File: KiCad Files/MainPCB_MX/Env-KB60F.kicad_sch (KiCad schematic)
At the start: 157 parts, among them J1 Conn_01x04, SW1 EVQ-P7A01P, U1 Pico

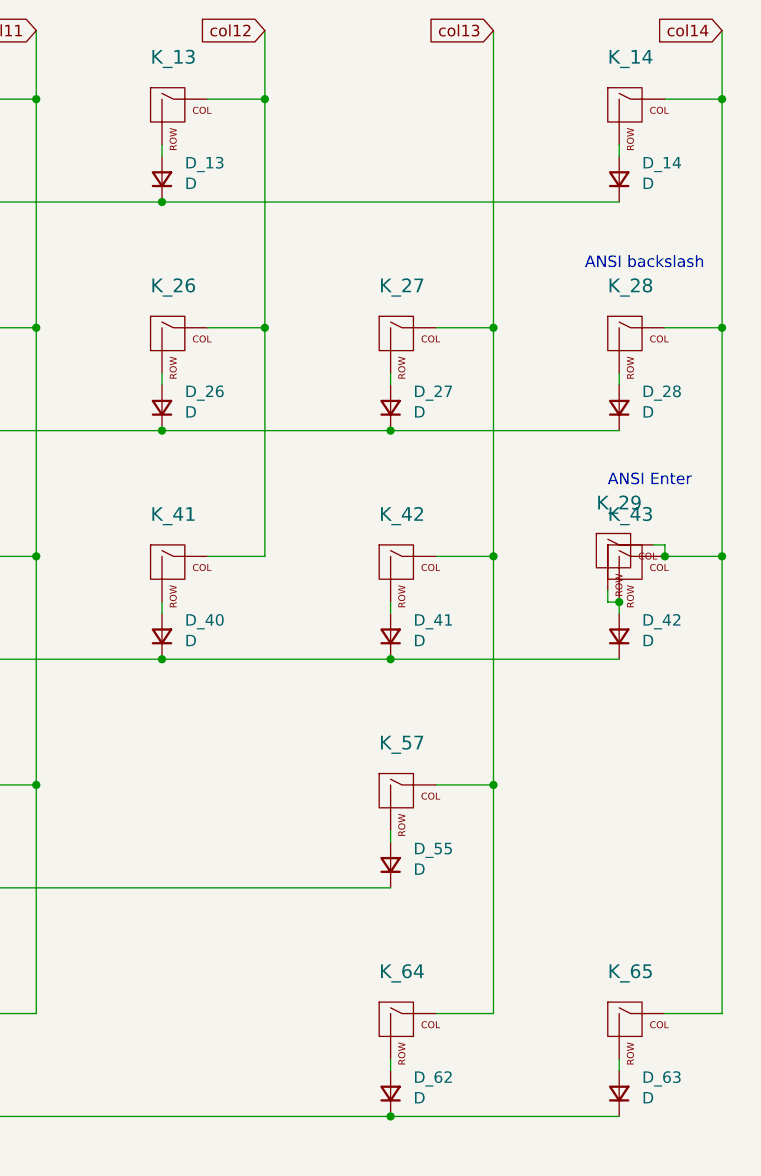
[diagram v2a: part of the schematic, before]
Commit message: added split backspace and right shift
backspace is 1u+1u and right shift is 1.75u + 1u.
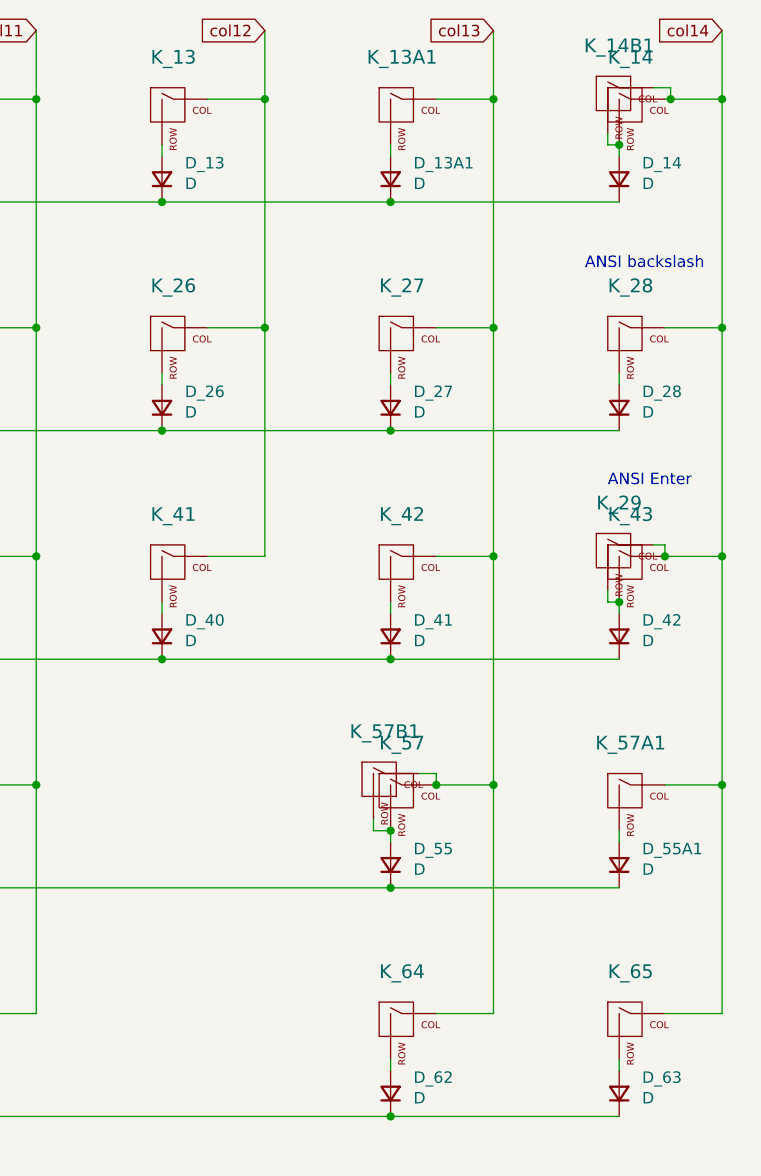
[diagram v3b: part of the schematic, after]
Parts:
- added D_13A1, D_55A1: D, Diode_THT:D_DO-35_SOD27_P7.62mm_Horizontal, symbol Device:D_Small
- added K_13A1, K_14B1, K_57A1: KEYSW, MX_Only:MXOnly-1U-NoLED, symbol MX_Alps_Hybrid:MX-NoLED
- added K_57B1: KEYSW, MX_Only:MXOnly-1.75U-NoLED, symbol MX_Alps_Hybrid:MX-NoLED
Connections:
- net col13: now also K_13A1.1 (COL), K_57B1.1 (COL)
- net col14: now also K_14B1.1 (COL), K_57A1.1 (COL)
- net row0: now also D_13A1.1 (K)
- net row3: now also D_55A1.1 (K)
- net at D_14.2 (A), K_14.2 (ROW): now also K_14B1.2 (ROW)
- net at D_55.2 (A), K_57.2 (ROW): now also K_57B1.2 (ROW)
- new net: D_55A1.2 (A), K_57A1.2 (ROW)
- new net: D_13A1.2 (A), K_13A1.2 (ROW)

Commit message: updated MX version a tiny bit, might order and do a tiny kit run.
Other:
- note added: "split backspace"
- note added: "split right shift"

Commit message: various design work toward producing and making a case
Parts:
- 5.1K1, 5.1K2: value 5.1K 0402 Resistor -> 5.1K 1/4W Resistor
- D_1, D_10, D_11, D_12, D_13, D_13A1, D_14, D_15, D_16, D_17, D_18, D_19, D_2, D_20, D_21, D_22, D_23, D_24, D_25, D_26, D_27, D_28, D_29, D_3, D_30, D_31, D_32, D_33, D_34, D_35, D_36, D_37, D_38, D_39, D_4, D_40, D_41, D_42, D_43, D_44, D_45, D_46, D_47, D_48, D_49, D_5, D_50, D_51, D_52, D_53, D_54, D_55, D_55A1, D_56, D_57, D_58, D_59, D_590, D_591, D_6, D_60, D_61, D_62, D_63, D_7, D_8, D_9: value D -> 1n4148

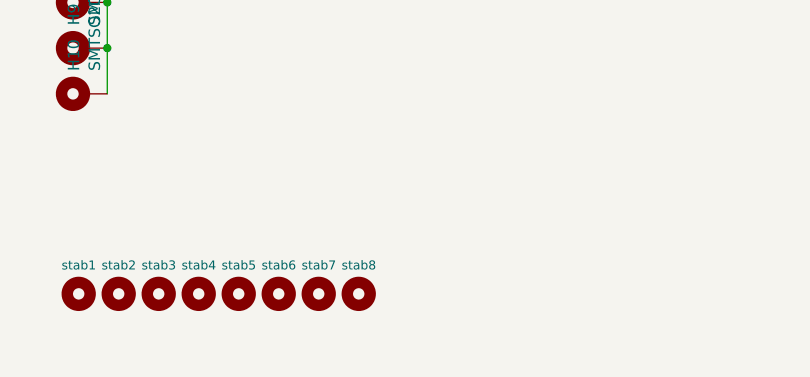
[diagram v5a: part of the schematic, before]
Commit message: fixed issues with alignment
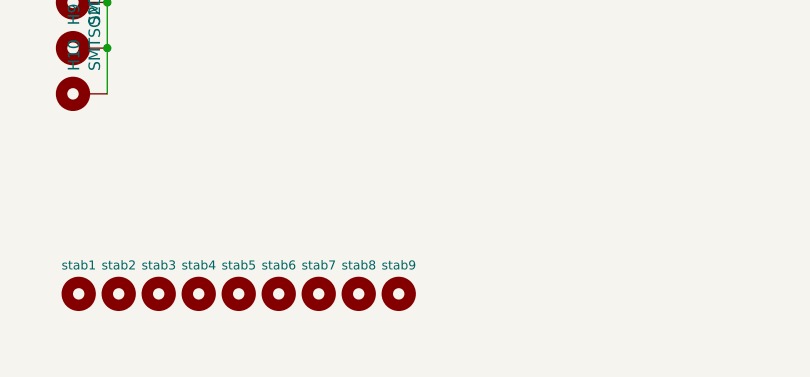
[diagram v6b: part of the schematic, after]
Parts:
- added stab9: MX Stabilizer, Mounting_Keyboard_Stabilizer:Stabilizer_Cherry_MX_6.25u, symbol Mechanical:MountingHole
